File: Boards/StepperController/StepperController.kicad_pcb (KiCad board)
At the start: 2 copper layers, 160 x 100 mm, 196 parts, among them IC1 ATMEGA645A-A, J1 I2C, J2 SPI_Extern, J3 ISP, J4 Reference, J5 Display, J6 Ext, J7 Spindle, P1 Power, P10 CONN_Z, P2 Cover, P3 USB_B, P4 Relay2, P5 Relay1, P6 Emer_Off, P8 CONN_X, P9 CONN_Y, Q1 BC817-40, Q2 BC817-40, Q3 BC817-40, Q4 BC817-40, Q5 BC817-40, Q6 BC807-40, Q7 BC807-40, Q8 BC817-40, SW2 SW_1, SW3 SW_2, U1 LM2576S-5, U2 74HC11, U3 FT232RL, U4 74HC08, U5 TMC2660, U6 TMC2660, U7 TMC2660, X1 16MHz, Y1 16MHz

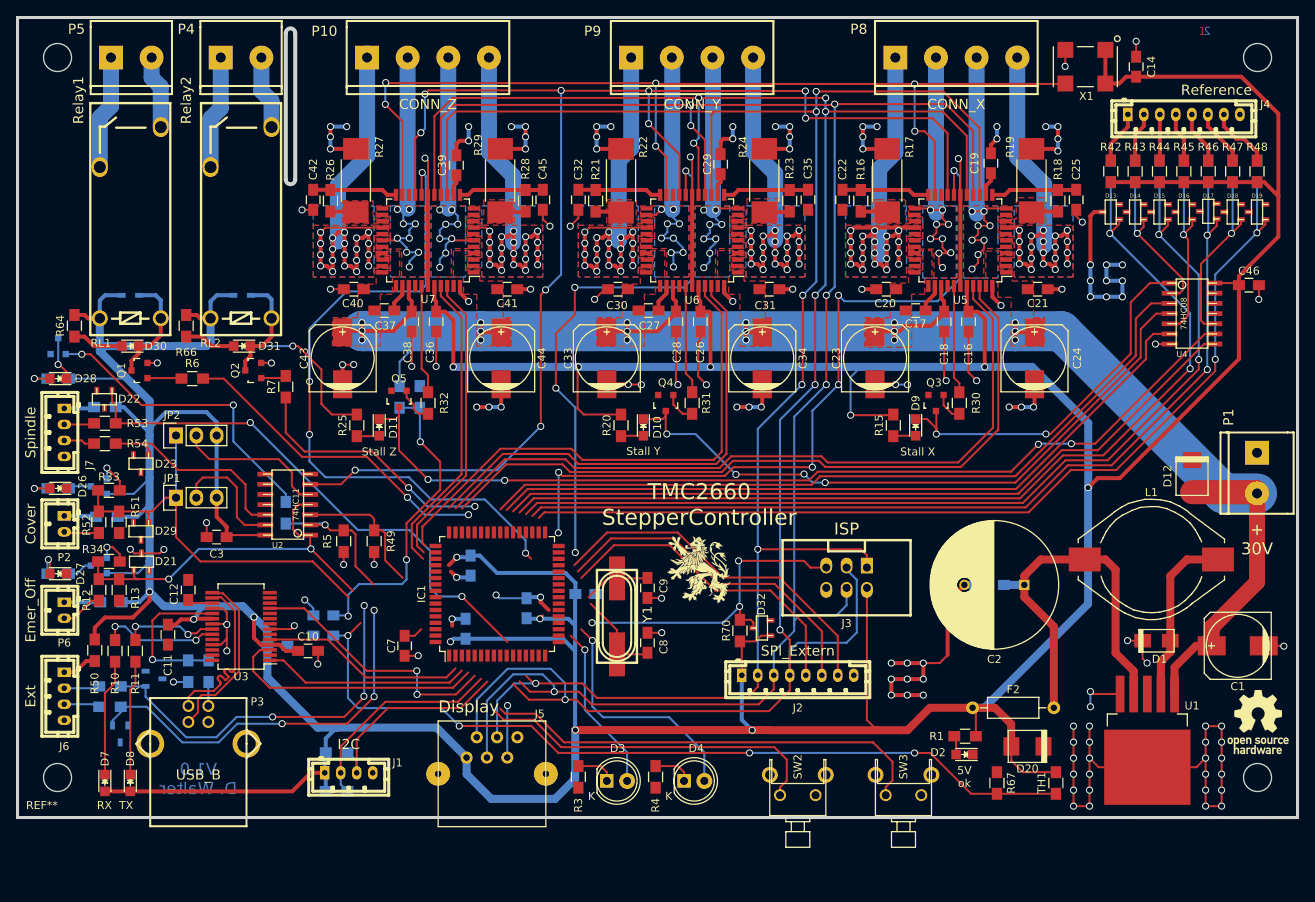
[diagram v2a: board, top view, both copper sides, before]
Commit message: Added Connector for Buttons & Emergency Off for Relays
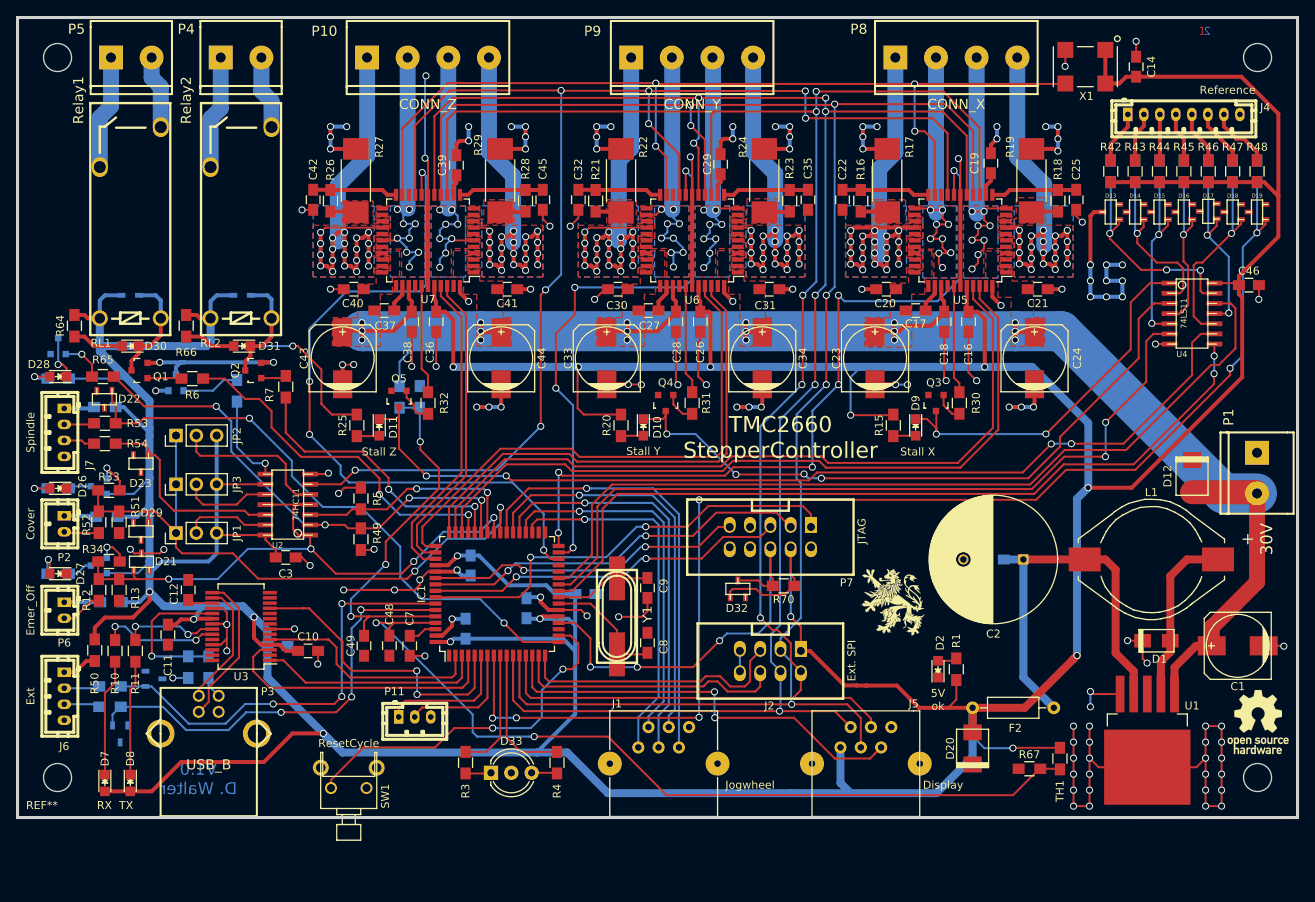
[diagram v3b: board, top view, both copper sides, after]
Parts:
- removed D3: LED_Gn, LEDs:LED-5MM
- removed D4: LED_Rd, LEDs:LED-5MM
- removed J3: ISP, w_conn_strip:vasch_strip_3x2
- removed R56, R57: 4k7, Resistors_SMD:R_0805_HandSoldering
- removed SW2: SW_1, SW0773:SW_0773
- removed SW3: SW_2, SW0773:SW_0773
- added D33: Led_x2, LEDs:LED_D5.0mm-3, F.Cu at (123.2, 147.3)
- added JP3: JUMPER3, Pin_Headers:Pin_Header_Straight_1x03_Pitch2.54mm, F.Cu at (83.8, 111.3)
- added P11: Buttons, w_conn_jst-ph:b3b-ph-kl, F.Cu at (113.7, 140.3)
- added P7: JTAG, w_conn_strip:vasch_strip_5x2, F.Cu at (158.1, 117.9)
- added Q9: BC817-40, TO_SOT_Packages_SMD:SOT-23, B.Cu at (83.8, 98.6)
- added R35: 1k, Resistors_SMD:R_0805_HandSoldering, B.Cu at (91.4, 99.6)
- added SW1: ResetCycle, SW0773:SW_0773, F.Cu at (105.4, 149.2)
- C48, C49, R65: moved to F.Cu
- IC1: value ATMEGA645A-A -> ATMEGA128-A
- J1: value I2C -> Jog; footprint w_conn_jst-ph:b4b-ph-kl -> Connect:RJ12_E
- J2: footprint w_conn_jst-ph:b8b-ph-kl -> w_conn_strip:vasch_strip_4x2
- JP1, JP2: footprint Pin_Headers:Pin_Header_Straight_1x03 -> Pin_Headers:Pin_Header_Straight_1x03_Pitch2.54mm
- U4: value 74HC08 -> 74LS11
- moved J5 46.8 mm to (170.2, 150.5)
- moved J1 36.3 mm to (141.6, 144.1)
- moved R65 28.5 mm to (74.7, 97.8), turned to 0 degrees
- moved G*** 24.6 mm to (173.5, 126.0)
- moved R3 14.2 mm to (120.0, 146.1)
- moved R4 12.4 mm to (131.4, 146.1)
- moved D2 11.2 mm to (179.1, 134.4), turned to 90 degrees
- moved C3 9.00 mm to (97.5, 120.4), turned to 0 degrees
- moved R1 8.45 mm to (181.4, 134.4), turned to 90 degrees
- moved C48 8.35 mm to (110.5, 131.4), turned to 270 degrees
- moved R70 7.81 mm to (159.8, 124.0), turned to 180 degrees
- moved D20 6.86 mm to (183.4, 144.3), turned to 270 degrees
- moved C49 6.35 mm to (107.3, 131.4), turned to 270 degrees
- moved R5 5.75 mm to (106.9, 113.0), turned to 90 degrees
- moved D32 5.74 mm to (154.1, 124.3), turned to 0 degrees
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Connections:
- IC1 pad 10: /Interface/CS_Disp -> /Controller/LED2
- IC1 pad 14: (no net) -> /Interface/CS_Disp
- IC1 pad 15: (no net) -> /Controller/CS_Ext1
- IC1 pad 16: (no net) -> /Controller/CS_Ext2
- IC1 pad 18: /Controller/LED1 -> Net-(IC1-Pad18)
- IC1 pad 19: /Controller/LED2 -> (no net)
- IC1 pad 25: (no net) -> Net-(IC1-Pad25)
- IC1 pad 26: (no net) -> Net-(IC1-Pad26)
- IC1 pad 27: /Controller/CS_Ext1 -> Net-(IC1-Pad27)
- IC1 pad 28: /Controller/CS_Ext2 -> (no net)
- IC1 pad 29: /Controller/CS_Ext3 -> (no net)
- IC1 pad 34: /Interface/Ref_T1 -> (no net)
- IC1 pad 35: /Controller/Ref_Z1 -> /Controller/JogA
- IC1 pad 36: /Controller/Ref_Y1 -> /Controller/JogB
- IC1 pad 37: /Controller/Ref_X1 -> /Controller/JogX
- IC1 pad 38: /Controller/RefZ2 -> /Controller/JogY
- IC1 pad 39: /Controller/RefY2 -> /Controller/JogZ
- IC1 pad 40: /Controller/RefX2 -> /Controller/Cover
- IC1 pad 41: (no net) -> /Controller/Emergency_Off
- IC1 pad 42: (no net) -> /Controller/Enable
- IC1 pad 43: (no net) -> /Interface/Spindle_Enable
- IC1 pad 54: /Controller/Enable -> Net-(IC1-Pad54)
- IC1 pad 55: /Interface/Spindle_Enable -> Net-(IC1-Pad55)
- IC1 pad 56: /Controller/Emergency_Off -> Net-(IC1-Pad56)
- IC1 pad 57: /Controller/Cover -> Net-(IC1-Pad57)
- IC1 pad 6: /Controller/SCL -> /Controller/FeedHold
- IC1 pad 7: /Controller/SDA -> /Controller/CycleStart
- IC1 pad 8: /Controller/Button1 -> /Interface/Ref_T1
- IC1 pad 9: /Controller/Button2 -> /Controller/LED1
- J1 pad 1: +5V -> /Controller/JogA
- J1 pad 2: /Controller/SCL -> /Controller/JogB
- J1 pad 3: /Controller/SDA -> /Controller/JogX
- J1 pad 4: GND -> /Controller/JogY
- J2 pad 5: /Controller/CS_Ext1 -> /Controller/CS_Ext2
- J2 pad 6: /Controller/CS_Ext2 -> /Controller/CS_Ext1
- J2 pad 7: /Controller/CS_Ext3 -> GND
- Q1 pad 2: GND -> Net-(Q1-Pad2)
- Q2 pad 2: GND -> Net-(Q1-Pad2)
- R3 pad 1: GND -> Net-(D33-Pad1)
- R3 pad 2: Net-(D3-Pad1) -> /Controller/LED1
- R4 pad 1: GND -> Net-(D33-Pad3)
- R4 pad 2: Net-(D4-Pad1) -> /Controller/LED2
- R49 pad 1: /Controller/Enable -> GND
- R49 pad 2: GND -> /Interface/Spindle_Enable
- R5 pad 1: /Interface/Spindle_Enable -> /Controller/Enable
- U2 pad 10: (no net) -> Net-(JP3-Pad2)
- U2 pad 11: (no net) -> /Controller/Emergency_Off
- U2 pad 8: (no net) -> Net-(R35-Pad2)
- U2 pad 9: (no net) -> +5V
- U4 pad 11: (no net) -> /Controller/Ref_Z1
- U4 pad 12: (no net) -> Net-(IC1-Pad27)
- U4 pad 13: (no net) -> /Controller/Ref_X1
- U4 pad 3: /Controller/RefX2 -> /Controller/Stall_Y
- U4 pad 4: /Controller/Stall_Y -> /Controller/Ref_Y2
- U4 pad 5: /Controller/Ref_Y2 -> /Controller/Ref_Y1
- U4 pad 6: /Controller/RefY2 -> Net-(IC1-Pad26)
- U4 pad 8: /Controller/RefZ2 -> Net-(IC1-Pad25)
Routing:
- net Net-(IC1-Pad27): track 0.00 -> 108.1 mm
- net Net-(IC1-Pad25): track 0.00 -> 101.4 mm, vias 0 -> 2
- net Net-(IC1-Pad26): track 0.00 -> 98.6 mm, vias 0 -> 2
- net /Controller/RefX2: track 97.1 -> 0.00 mm
- net /Controller/Ref_Y1: track 119.5 -> 22.7 mm
- net /Controller/RefZ2: track 96.3 -> 0.00 mm
- net /Controller/Ref_Z1: track 118.0 -> 21.9 mm
- net /Controller/Ref_X1: track 120.7 -> 26.4 mm, vias 2 -> 3
- net /Controller/RefY2: track 93.3 -> 0.00 mm
- net /Controller/Button2: track 56.3 -> 0.00 mm
- net /Controller/JogZ: track 0.00 -> 55.9 mm, vias 0 -> 1
- net Net-(IC1-Pad57): track 0.00 -> 55.8 mm, vias 0 -> 2
- net /Controller/JogX: track 0.00 -> 51.2 mm, vias 0 -> 1
- net /Controller/JogY: track 0.00 -> 51.2 mm, vias 0 -> 1
- net Net-(IC1-Pad55): track 0.00 -> 48.9 mm, vias 0 -> 2
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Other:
- board text added: "5V"
- board text added: "CycleStart"
- board text added: "Enable"
- board text added: "Ext. 1"
- board text added: "Ext. 2"
- board text added: "Ext. SPI"
- board text added: "FeedHold"
- board text added: "GND"
- board text added: "JTAG"
- board text added: "Jogwheel"
- board text added: "PWM"
- board text added: "Switch"
- board text removed: "ISP"

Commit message: Final Version for Manufacturing
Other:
- board text added: "Check Cover"
- board text added: "Ignore Cover"
- board text added: "Relais"
- board text added: "Spindle"
- board text added: "Steppers"
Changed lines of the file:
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@@
     (area 62.758 41.496 242.498286 156.803601)
     (thickness 1.6)
-    (drawings 33)
+    (drawings 42)
     (tracks 2554)
     (zones 0)
@@
   )
   (setup
-    (last_trace_width 1)
+    (last_trace_width 0.254)
     (user_trace_width 0.3)
     (user_trace_width 0.4)
@@
     )
   )
+  (gr_arc (start 98.044 74.93) (end 97.536 74.93) (angle -180) (layer Edge.Cuts) (width 0.5))
+  (gr_line (start 97.536 55.88) (end 97.536 74.93) (layer Edge.Cuts) (width 0.5))
+  (gr_arc (start 98.044 55.88) (end 97.536 55.88) (angle 180) (layer Edge.Cuts) (width 0.5))
+  (gr_line (start 98.552 55.88) (end 98.552 74.93) (layer Edge.Cuts) (width 0.5))
+  (gr_text Steppers (at 80.01 117.348) (layer B.SilkS)
+    (effects (font (size 0.8 0.8) (thickness 0.15)) (justify mirror))
+  )
+  (gr_text Relais (at 80.772 111.252) (layer B.SilkS)
+    (effects (font (size 0.8 0.8) (thickness 0.15)) (justify mirror))
+  )
+  (gr_text Spindle (at 80.518 105.156) (layer B.SilkS)
+    (effects (font (size 0.8 0.8) (thickness 0.15)) (justify mirror))
+  )
+  (gr_text "Check Cover" (at 83.82 122.428 90) (layer B.SilkS)
+    (effects (font (size 0.8 0.8) (thickness 0.15)) (justify mirror))
+  )
+  (gr_text "Ignore Cover" (at 88.9 122.428 90) (layer B.SilkS)
+    (effects (font (size 0.8 0.8) (thickness 0.15)) (justify mirror))
+  )
   (gr_text GND (at 68.58 107.696) (layer B.SilkS)

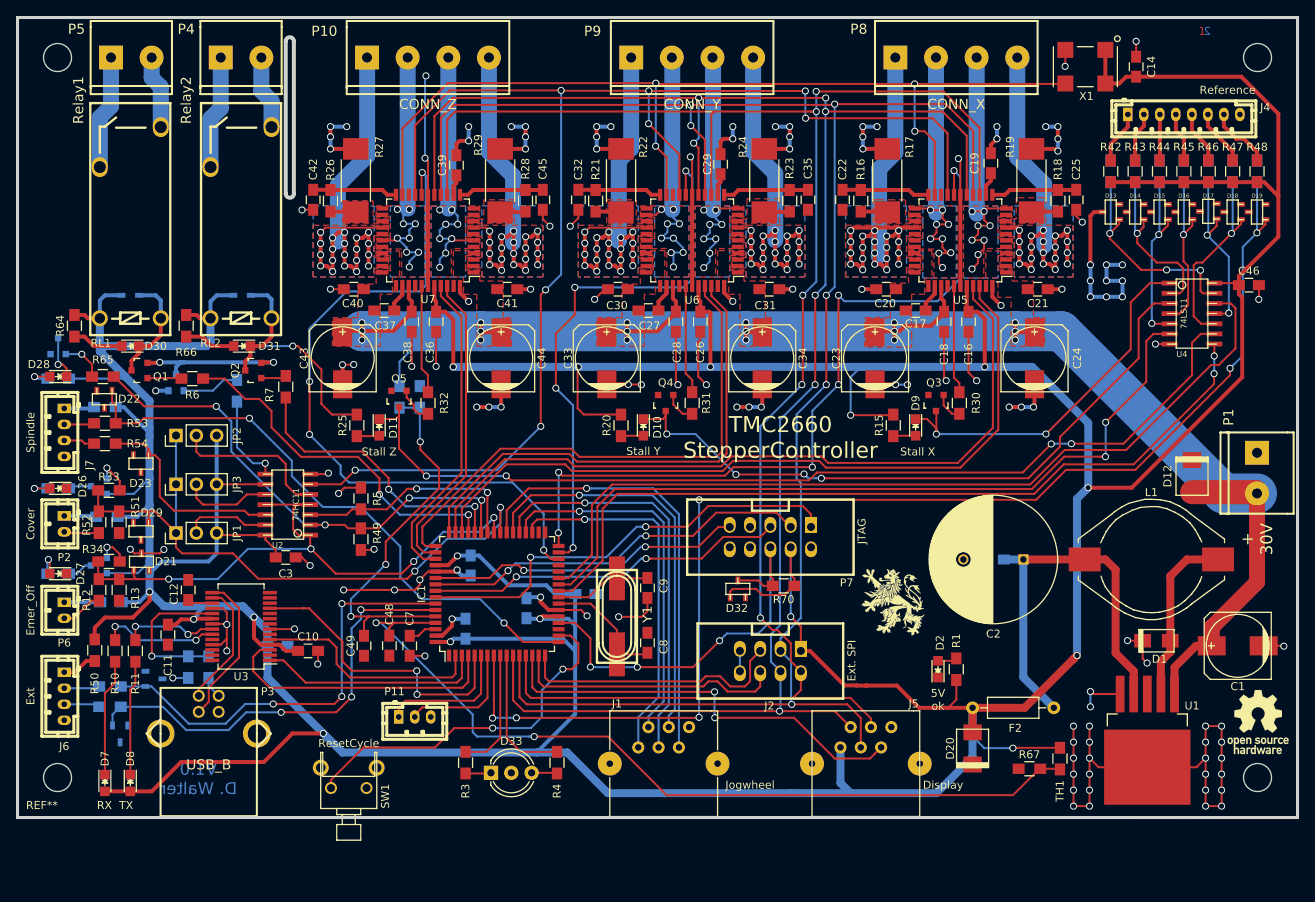
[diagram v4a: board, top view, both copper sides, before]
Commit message: Added Buffering for Inputs
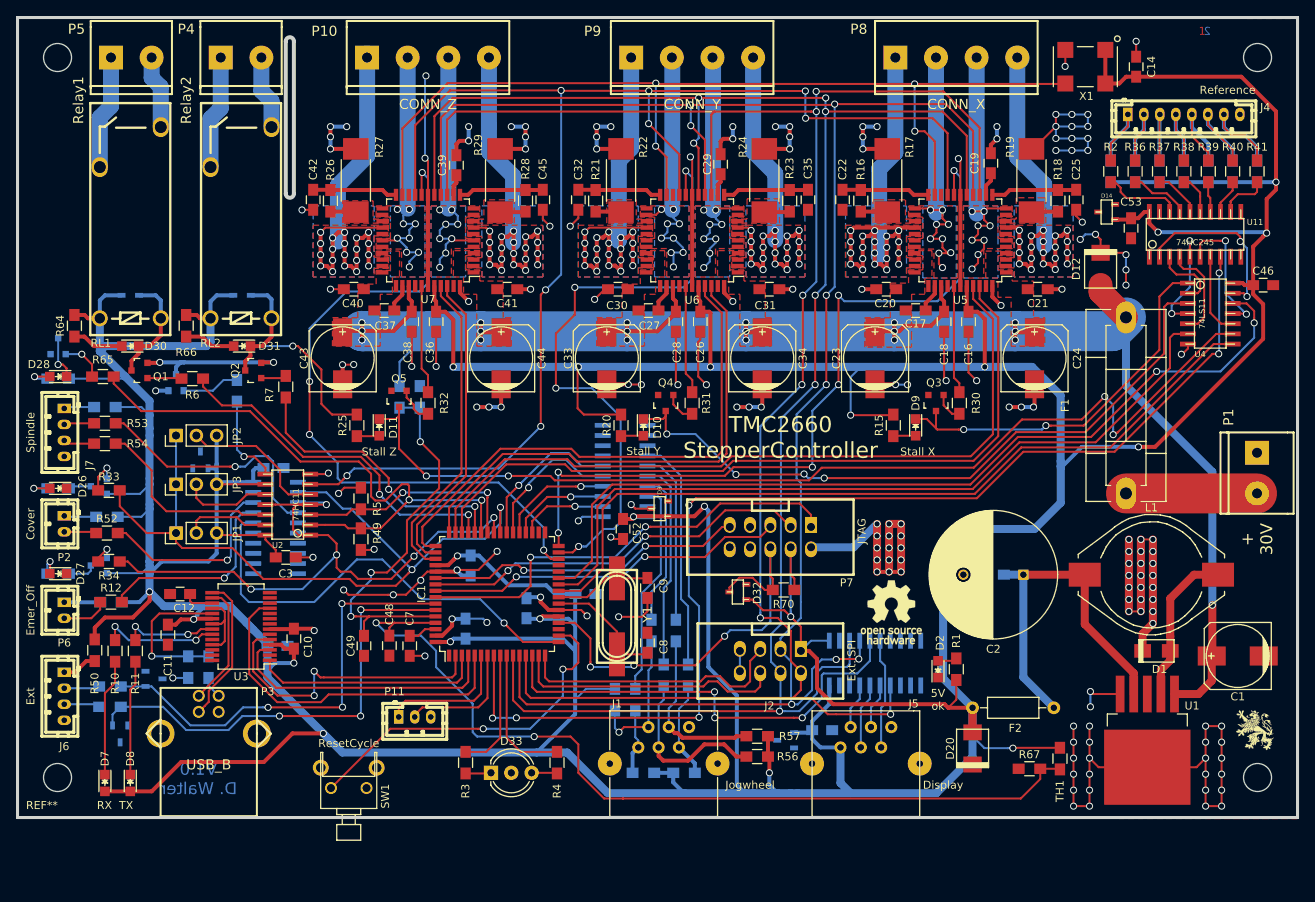
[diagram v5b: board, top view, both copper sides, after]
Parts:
- removed D15, D16, D17, D18, D19, D21, D22, D23, D29: ZMY5,6, w_smd_trans:sot23
- added C50: 100nF, Capacitors_SMD:C_0805_HandSoldering, B.Cu at (96.0, 109.2)
- added C51: 100nF, Capacitors_SMD:C_0805_HandSoldering, B.Cu at (164.6, 142.0)
- added C52: 100nF, Capacitors_SMD:C_0805_HandSoldering, F.Cu at (139.7, 116.8)
- added C53: 100nF, Capacitors_SMD:C_0805_HandSoldering, F.Cu at (203.2, 79.2)
- added D3: ZMY5,6, w_smd_trans:sot23, F.Cu at (144.3, 114.3)
- added D4: ZMY5,6, w_smd_trans:sot23, B.Cu at (86.9, 108.2)
- added F1: 10AT, Fuse_Holders_and_Fuses:Fuseholder5x20_horiz_SemiClosed_Casing10x25mm, F.Cu at (202.6, 112.4)
- added R56: 4k7, Resistors_SMD:R_0805_HandSoldering, F.Cu at (156.5, 145.3)
- added R57: 4k7, Resistors_SMD:R_0805_HandSoldering, F.Cu at (156.5, 142.7)
- added R71: 4k7, Resistors_SMD:R_0805_HandSoldering, B.Cu at (147.3, 147.3)
- added R72: 100R, Resistors_SMD:R_0805_HandSoldering, B.Cu at (141.2, 138.2)
- added R73: 100R, Resistors_SMD:R_0805_HandSoldering, B.Cu at (143.3, 129.5)
- added R74: 100R, Resistors_SMD:R_0805_HandSoldering, B.Cu at (144.8, 135.1)
- added R75: 100R, Resistors_SMD:R_0805_HandSoldering, B.Cu at (146.3, 129.5)
- added R76: 100R, Resistors_SMD:R_0805_HandSoldering, B.Cu at (147.8, 135.1)
- added U10: 74HC245, SO20:so-20, B.Cu at (96.3, 116.7)
- added U11: 74HC245, SO20:so-20, F.Cu at (211.2, 80.0)
- added U8: 74HC245, SO20:so-20, B.Cu at (140.0, 109.6)
- added U9: 74HC245, SO20:so-20, B.Cu at (171.2, 133.6)
- D13, R42, R43, R44, R45, R46, R47, R48: moved to B.Cu
- R13, R51: value 3k6 -> 4k7; moved to B.Cu
- R2, R36, R37, R38, R39, R40, R41: moved to F.Cu
- moved D13 77.5 mm to (160.0, 143.3), turned to 270 degrees
- moved R13 69.4 mm to (142.2, 147.3), turned to 180 degrees
- moved R51 65.8 mm to (138.7, 138.2), turned to 270 degrees
- moved G*** 48.0 mm to (218.7, 142.0)
- moved REF*** 47.9 mm to (173.2, 127.3)
- moved D12 28.3 mm to (199.4, 84.3)
- moved D14 3.56 mm to (200.2, 77.2)
- moved C10 2.34 mm to (98.6, 130.6), turned to 90 degrees
- moved U4 2.29 mm to (213.1, 89.9)
- moved R12 2.16 mm to (75.7, 126.0), turned to 180 degrees
- moved C15 1.91 mm to (186.1, 122.6)
- moved C2 1.91 mm to (189.7, 122.6)
- moved L1 1.91 mm to (205.7, 122.6)
- moved C46 1.78 mm to (219.7, 86.4)
- moved R52 1.69 mm to (75.2, 117.3), turned to 180 degrees
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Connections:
- D13 pad 1: /Controller/Ref_X1 -> +5V
- D14 pad 1: /Controller/Ref_X2 -> +5V
- J1 pad 1: /Controller/JogA -> Net-(J1-Pad1)
- J1 pad 2: /Controller/JogB -> Net-(J1-Pad2)
- J1 pad 3: /Controller/JogX -> Net-(J1-Pad3)
- J1 pad 4: /Controller/JogY -> Net-(J1-Pad4)
- J1 pad 5: /Controller/JogZ -> Net-(J1-Pad5)
- J5 pad 2: /Controller/SCK -> Net-(J5-Pad2)
- J5 pad 3: /Controller/SDI -> Net-(J5-Pad3)
- J5 pad 4: /Controller/SDO -> Net-(J5-Pad4)
- J5 pad 5: /Interface/CS_Disp -> Net-(J5-Pad5)
- P1 pad 2: VSA -> Net-(F1-Pad1)
- R12 pad 1: /Controller/Emergency_Off -> Net-(R12-Pad1)
- R13 pad 1: GND -> +5V
- R13 pad 2: /Controller/Emergency_Off -> Net-(J1-Pad1)
- R2 pad 1: /Controller/Ref_X1 -> Net-(R2-Pad1)
- R33 pad 1: /Controller/Cover -> Net-(Q6-Pad1)
- R33 pad 2: Net-(Q6-Pad1) -> /Controller/Cover
- R34 pad 1: /Controller/Emergency_Off -> Net-(Q7-Pad1)
- R34 pad 2: Net-(Q7-Pad1) -> /Controller/Emergency_Off
- R36 pad 1: /Controller/Ref_X2 -> Net-(R36-Pad1)
- R37 pad 1: /Controller/Ref_Y1 -> Net-(R37-Pad1)
- R38 pad 1: /Controller/Ref_Y2 -> Net-(R38-Pad1)
- R39 pad 1: /Controller/Ref_Z1 -> Net-(R39-Pad1)
- R40 pad 1: /Controller/Ref_Z2 -> Net-(R40-Pad1)
- R41 pad 1: /Interface/Ref_T1 -> Net-(R41-Pad1)
- R51 pad 1: GND -> +5V
- R51 pad 2: /Controller/Cover -> Net-(J1-Pad2)
- R52 pad 1: /Controller/Cover -> Net-(R52-Pad1)
- R53 pad 1: /Controller/Spindle_PWM -> Net-(R53-Pad1)
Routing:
- net +5V: track 799.3 -> 918.2 mm, vias 17 -> 22
- net GND: track 395.0 -> 470.4 mm, vias 131 -> 168
- net /Controller/JogX: track 51.2 -> 14.1 mm
- net /Controller/JogZ: track 55.9 -> 19.4 mm
- net /Controller/JogA: track 46.2 -> 11.0 mm
- net /Controller/JogB: track 46.2 -> 12.5 mm
- net /Controller/JogY: track 51.2 -> 18.2 mm
- net Net-(R53-Pad1): track 0.00 -> 31.2 mm, vias 0 -> 1
- net Net-(R76-Pad1): track 0.00 -> 29.2 mm
- net Net-(R72-Pad1): track 0.00 -> 26.9 mm
- net Net-(R74-Pad1): track 0.00 -> 26.0 mm
- net Net-(R12-Pad1): track 0.00 -> 25.0 mm, vias 0 -> 1
- net Net-(R52-Pad1): track 0.00 -> 24.3 mm, vias 0 -> 1
- net Net-(J1-Pad3): track 0.00 -> 21.7 mm
- net Net-(R75-Pad1): track 0.00 -> 21.6 mm
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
